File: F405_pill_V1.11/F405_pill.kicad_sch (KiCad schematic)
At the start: 50 parts, among them J1 Conn_01x04_Male, J2 Conn_01x04_Male, J4 TYPE-C-31-M-12, U1 STM32F405RGTx, U2 TJA1050T/CM,118, U3 LM1117-3.3, U4 STM32F405_pill, U5 HT7550, Y1 Crystal_GND24

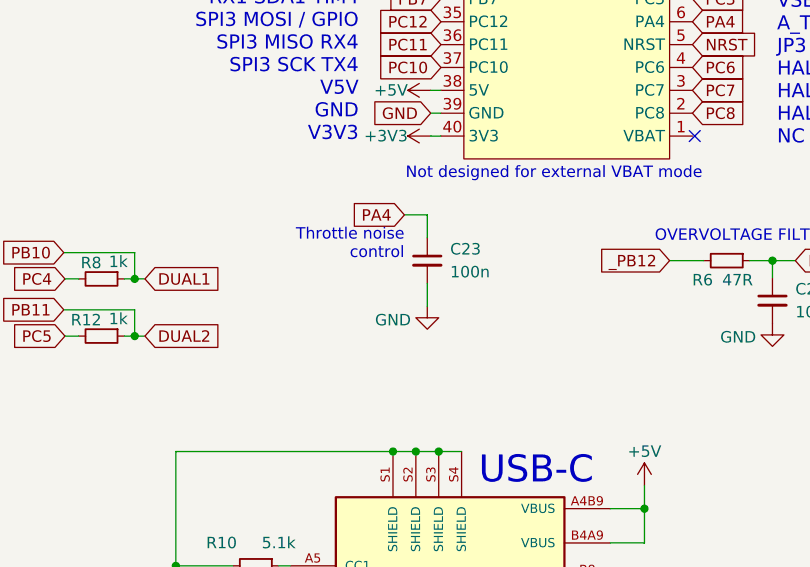
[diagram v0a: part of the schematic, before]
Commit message: changed V1.11 schematic
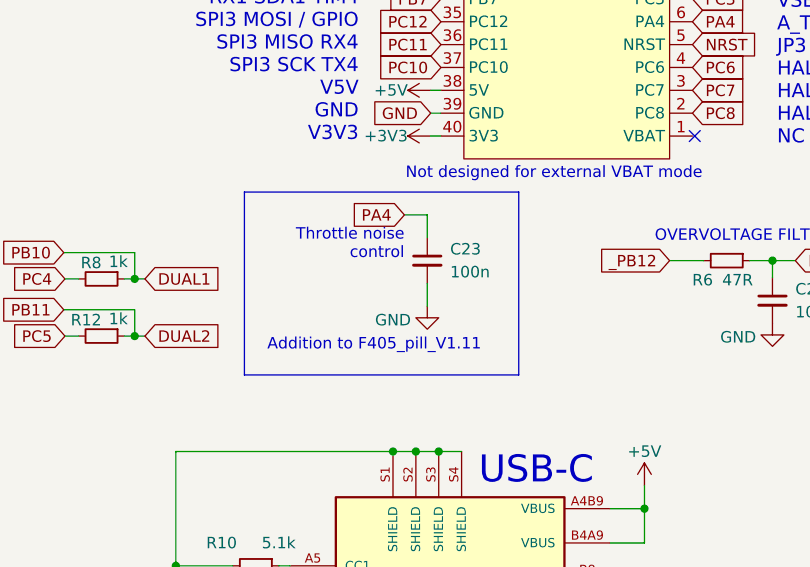
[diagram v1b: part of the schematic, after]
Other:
- note added: "Addition to F405_pill_V1.11"
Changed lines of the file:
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@@
     (stroke (width 0) (type default))
+  )
+  (rectangle (start 149.86 86.36) (end 180.34 106.68)
+    (stroke (width 0) (type default))
+    (fill (type none))
   )
   (text "MCU" (at 84.455 55.499 0)
@@
     (effects (font (size 1.27 1.27)) (justify left bottom))
   )
+  (text "Addition to F405_pill_V1.11" (at 152.4 104.14 0)
+    (effects (font (size 1.27 1.27)) (justify left bottom))
+  )

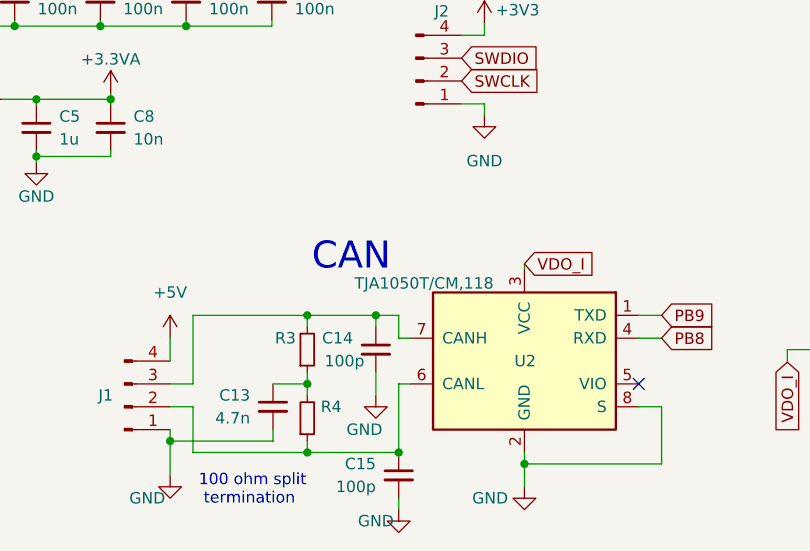
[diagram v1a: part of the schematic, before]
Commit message: added manufacturing files
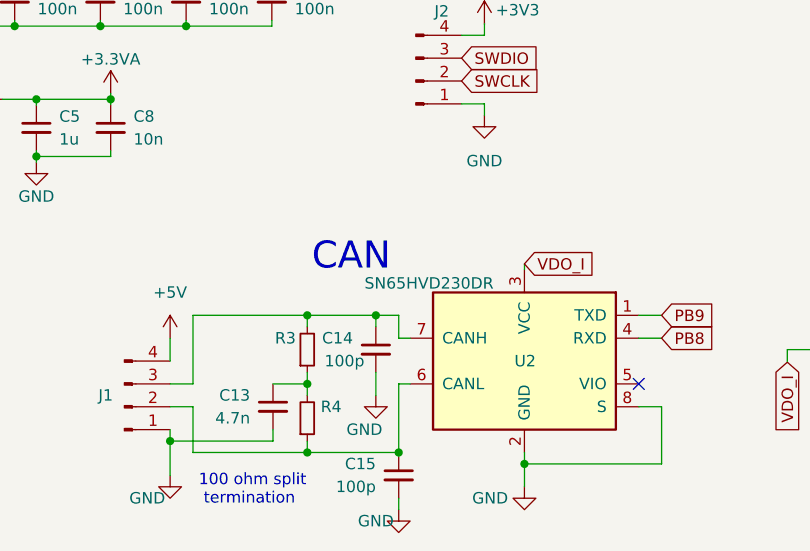
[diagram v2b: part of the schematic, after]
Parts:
- C16, C22: LCSC C962635 -> C1952781
- U2: value TJA1050T/CM,118 -> SN65HVD230DR; LCSC C6952 -> C12084
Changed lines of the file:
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@@
       (effects (font (size 1.27 1.27)) hide)
     )
-    (property "LCSC" "C962635" (at 127 169.291 0)
+    (property "LCSC" "C1952781" (at 127 169.291 0)
       (effects (font (size 1.27 1.27)) hide)
     )
@@
       (effects (font (size 1.27 1.27)) hide)
     )
-    (property "LCSC" "C962635" (at 246.634 140.97 0)
+    (property "LCSC" "C1952781" (at 246.634 140.97 0)
       (effects (font (size 1.27 1.27)) hide)
     )
@@
       (effects (font (size 1.27 1.27)) (justify left))
     )
-    (property "Value" " TJA1050T/CM,118" (at 89.916 158.496 0)
+    (property "Value" "SN65HVD230DR" (at 89.916 158.496 0)
       (effects (font (size 1.27 1.27)) (justify left))
     )
@@
       (effects (font (size 1.27 1.27)) hide)
     )
-    (property "LCSC" "C6952" (at 93.345 167.132 0)
-      (effects (font (size 1.27 1.27)) hide)
-    )
+    (property "LCSC" "C12084" (at 93.345 167.132 0)
+      (effects (font (size 1.27 1.27)) hide)
+    )
